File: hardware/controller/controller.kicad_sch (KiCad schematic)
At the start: 13 parts, among them J1 Conn_01x02_Pin, J2 Conn_01x02_Pin, J3 Conn_01x02_Pin, J4 Conn_01x02_Pin, SW1 SW_DIP_x01, U1 ESP32-S3-DEVKITC-1-N8R8

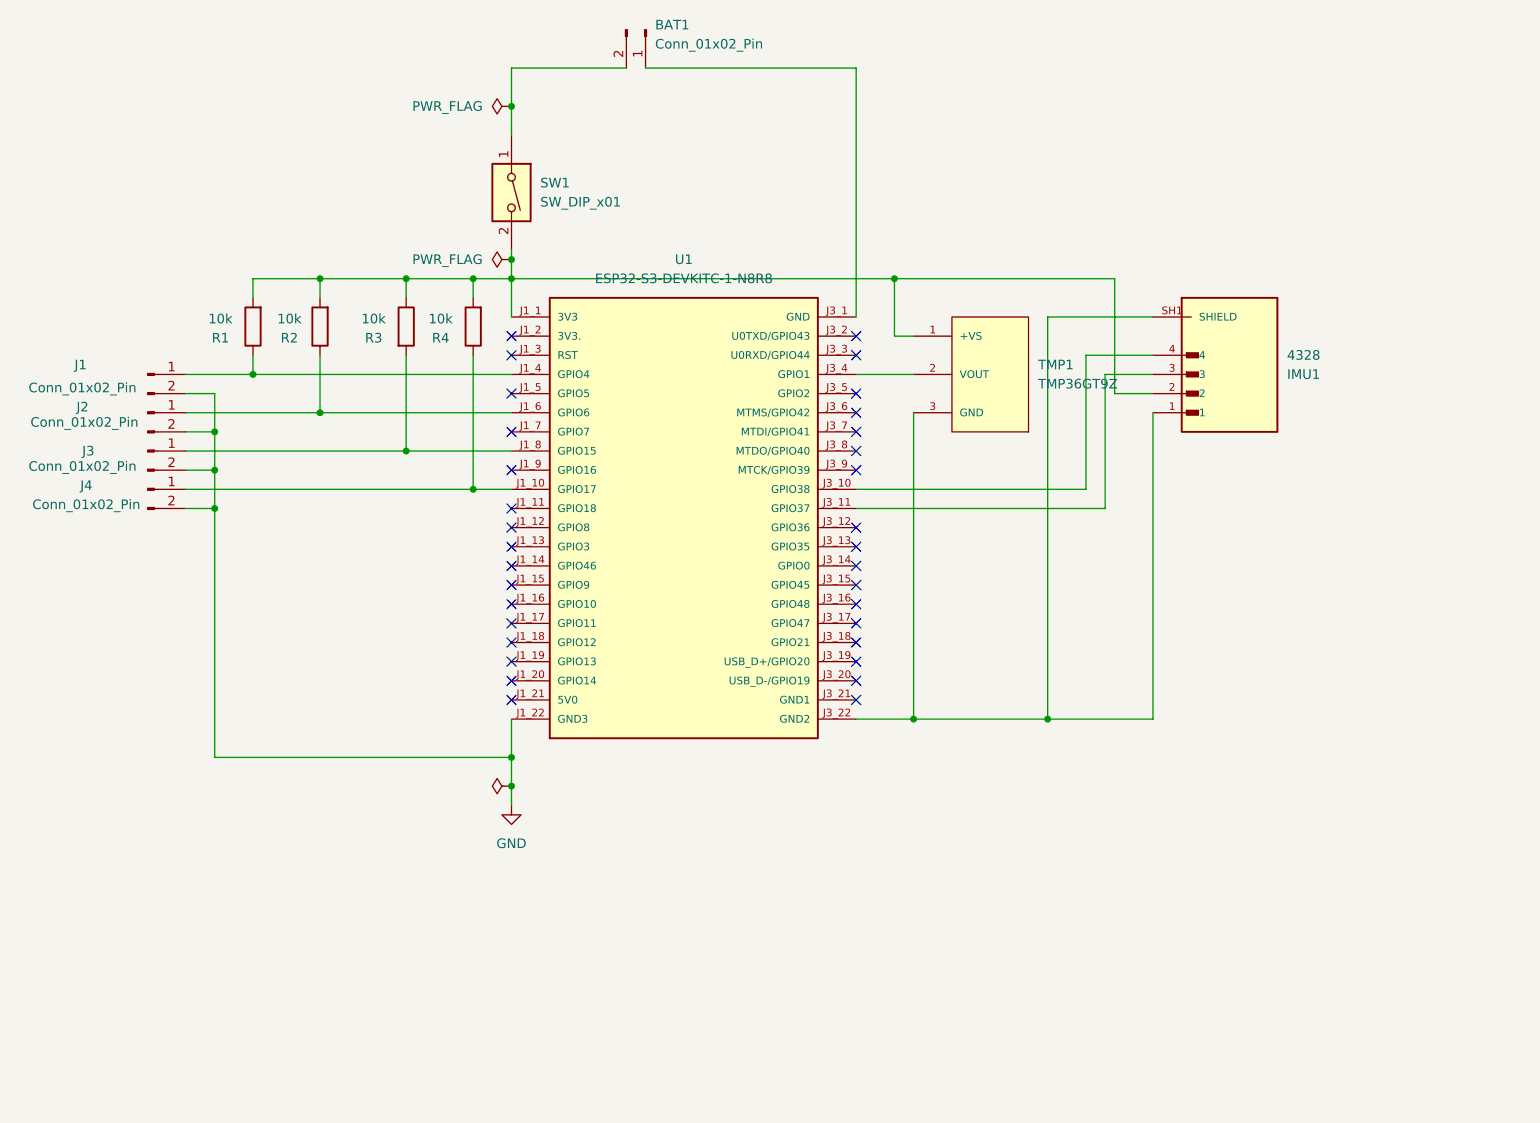
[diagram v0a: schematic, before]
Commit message: PCB Redesign for UWB Module
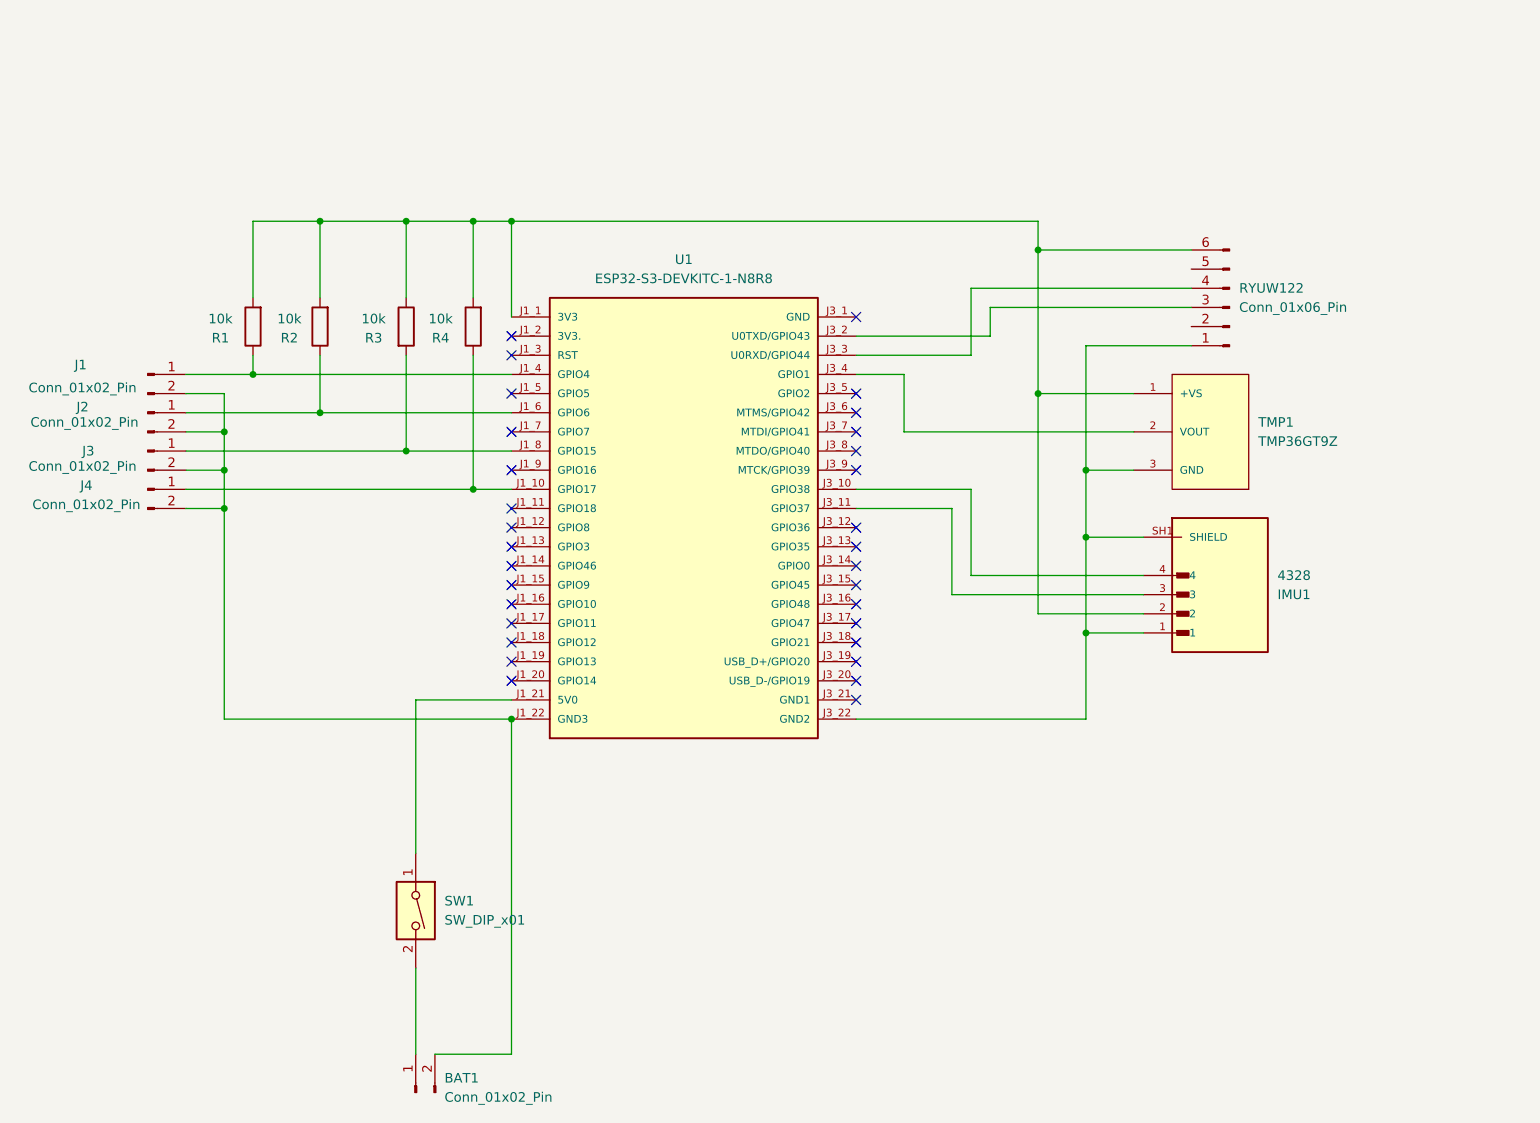
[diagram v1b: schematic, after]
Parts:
- added RYUW122: Conn_01x06_Pin, Connector_PinSocket_1.00mm:PinSocket_1x06_P1.00mm_Vertical, symbol Connector:Conn_01x06_Pin
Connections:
- net GND is gone; now on an unnamed net: J1.2 (Pin_2), J2.2 (Pin_2), J3.2 (Pin_2), J4.2 (Pin_2), U1.J1_22 (GND3)
- net at BAT1.1 (Pin_1): now also SW1.2; no longer U1.J3_1 (GND)
- net at BAT1.2 (Pin_2): no longer SW1.1
- net at IMU1.2, R1.2, R2.2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: now also RYUW122.6 (Pin_6); no longer SW1.2
- net at IMU1.1, IMU1.SH1 (SHIELD), IMU1.SH2 (SHIELD)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: now also RYUW122.1 (Pin_1)
- net at U1.J1_21 (5V0): now also SW1.1
- net at U1.J3_2 (U0TXD/GPIO43): now also RYUW122.3 (Pin_3)
- net at U1.J3_3 (U0RXD/GPIO44): now also RYUW122.4 (Pin_4)
- no-connect marks 33 -> 31
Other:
- moved on the sheet: BAT1, IMU1, SW1, TMP1

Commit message: adding all part ready for schem layout
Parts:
- removed BAT1: Conn_01x02_Pin, Connector_PinSocket_2.54mm:PinSocket_1x02_P2.54mm_Vertical, symbol Connector:Conn_01x02_Pin
- removed IMU1: 4328, 4328:ADAFRUIT_4328, symbol 4328:4328
- removed RYUW122: Conn_01x06_Pin, Connector_PinSocket_1.00mm:PinSocket_1x06_P1.00mm_Vertical, symbol Connector:Conn_01x06_Pin
- removed TMP1: TMP36GT9Z, TMP36GT9Z:TO92127P521H733-3, symbol TMP36GT9Z:TMP36GT9Z
- added J5: USB C Lipo Pins, symbol Connector:Conn_01x05_Pin
- added J6: IMU (x/y/z side), symbol Connector:Conn_01x06_Pin
- added J7: IMU (gnd/vdd side), symbol Connector:Conn_01x06_Pin
- added J8: UWB, symbol Connector:Conn_01x06_Pin
- added S1: Input Listener Switch, B3F-1000:SW_B3F-1000, symbol B3F-1000:B3F-1000
- SW1: value SW_DIP_x01 -> Power Switch
- U1: Description_1 The ESP32-S3-DEVKITC-1-N8R8 from Espressif Systems is a development board designed for RF, RFID, and wireless applications. It supports 802.11 b/g/n Wi-Fi and Bluetooth® 5.x (BLE) connectivity at 2.4GHz, making it ideal for IoT and wireless communication projects. This board is powered by the ESP32-S3-WROOM-1-N8R8 module, which features 8MB Quad SPI Flash and 8MB Octal SPI for efficient memory storage and processing. -> The ESP32-S3-DEVKITC-1-N8R8 from Espressif Systems is a development board designed for RF, RFID, and wireless applications. It supports 802.11 b/g/n Wi-Fi and Bluetooth® 5.x (BLE) connectivity at 2.4GHz, making it ideal for IoT and wireless communication projects. This board is powered by the ESP32-S3-WROOM-1-N8R8 module, which features 8MB Quad SPI Flash and 8MB Octal SPI for efficient memory storage and processing.
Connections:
- no-connect marks 31 -> 34
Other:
- note added: "Finger Sensors"
- note added: "Resistors for Finger Sensors"

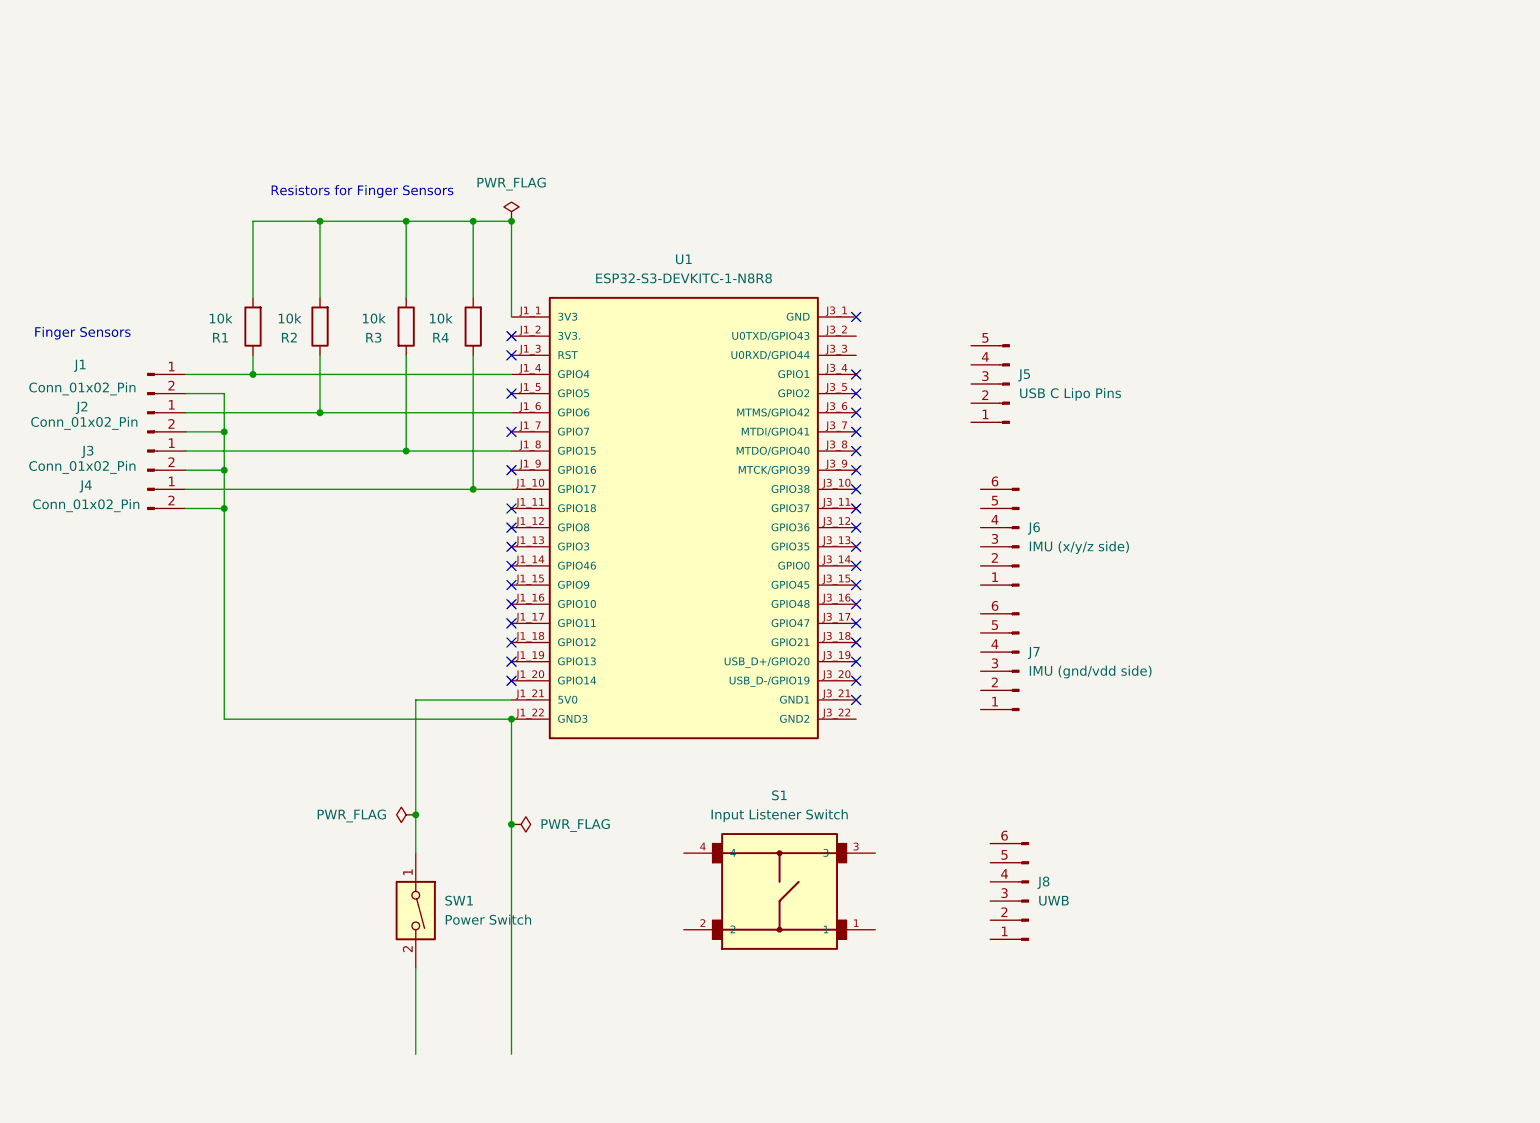
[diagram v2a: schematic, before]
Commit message: adding labels and swapping power switch on schem
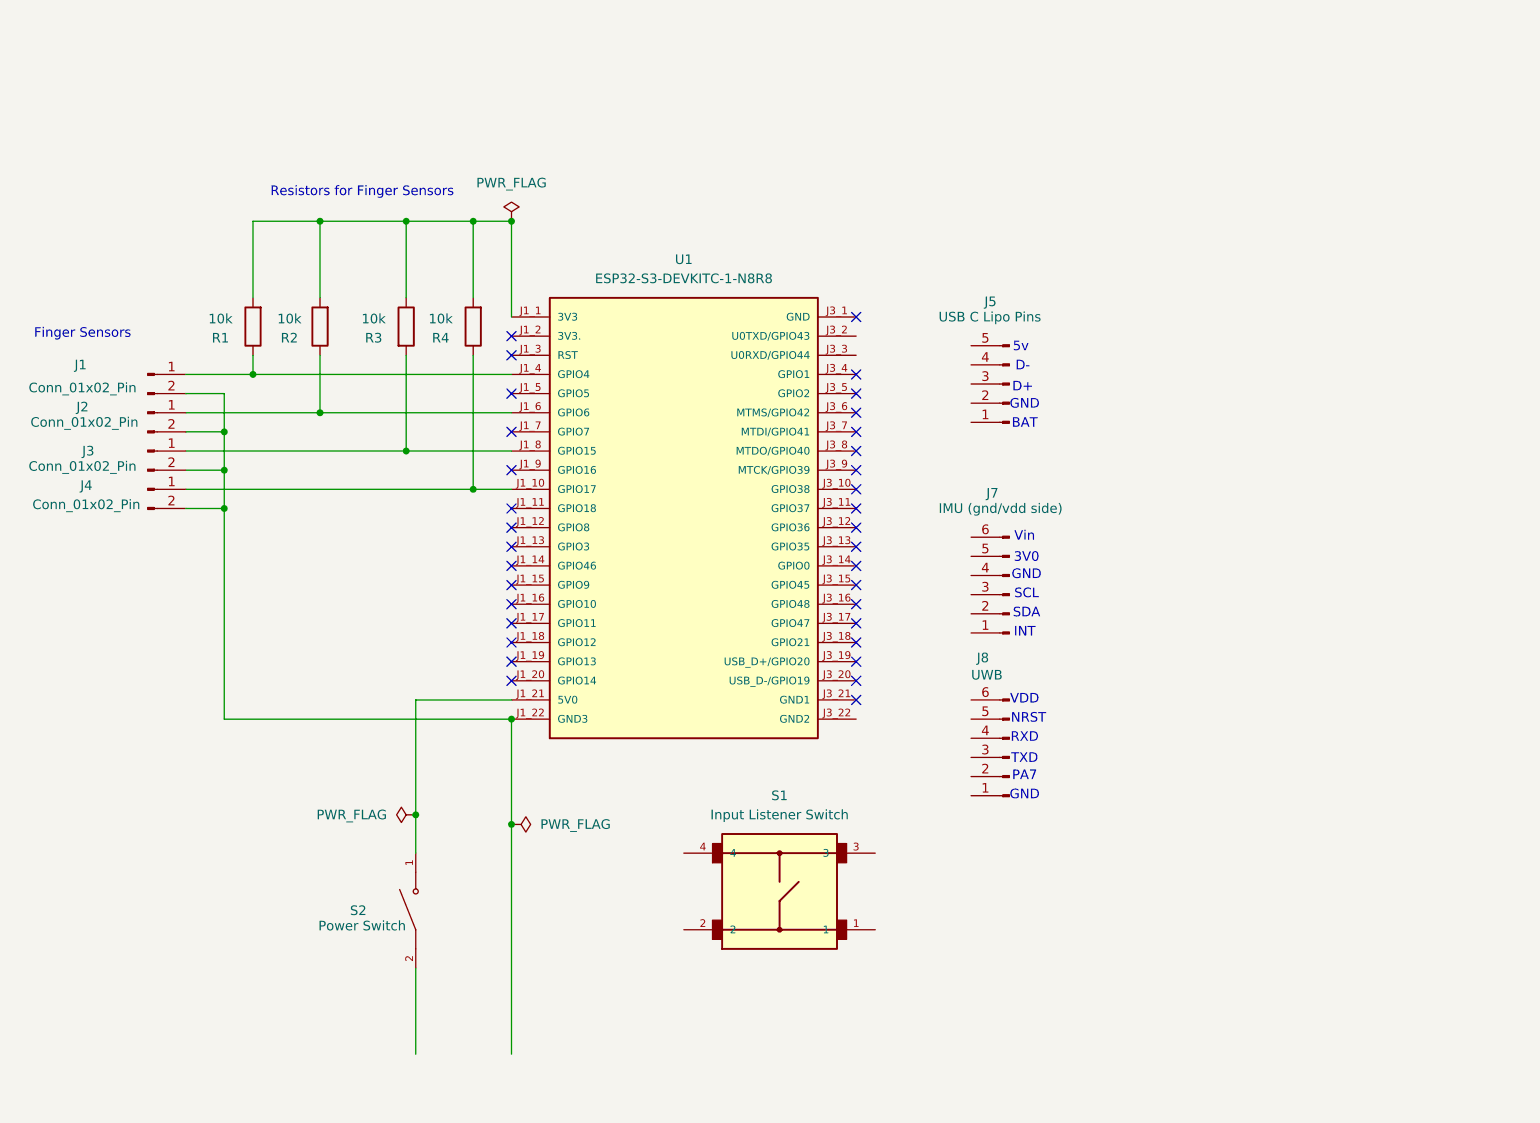
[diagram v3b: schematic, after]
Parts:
- removed J6: IMU (x/y/z side), symbol Connector:Conn_01x06_Pin
- removed SW1: Power Switch, Button_Switch_SMD:SW_SPST_SKQG_WithStem, symbol Switch:SW_DIP_x01
- added S2: Power Switch, GF-123-0054:SW_GF-123-0054, symbol GF-123-0054:GF-123-0054
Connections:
- net at U1.J1_21 (5V0): now also S2.1
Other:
- note added: "3V0"
- note added: "5v"
- note added: "BAT"
- note added: "D+"
- note added: "D-"
- note added: "GND"
- note added: "INT"
- note added: "NRST"
- note added: "PA7"
- note added: "RXD"
- note added: "SCL"
- note added: "SDA"
- note added: "TXD"
- note added: "VDD"
- note added: "Vin"
- moved on the sheet: J7, J8
